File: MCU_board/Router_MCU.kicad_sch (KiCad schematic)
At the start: 72 parts, among them J1 Header, T1 HY601742, U1 MYC-YT507H, U2 TPS54340, U3 LAN8720A, X1 B4B-XH, X2 B4B-XH, X3 B4B-XH, X4 B4B-XH, X5 B2B-XH, X6 TFP09-2-12B, X7 RJ45, Y1 25MHz

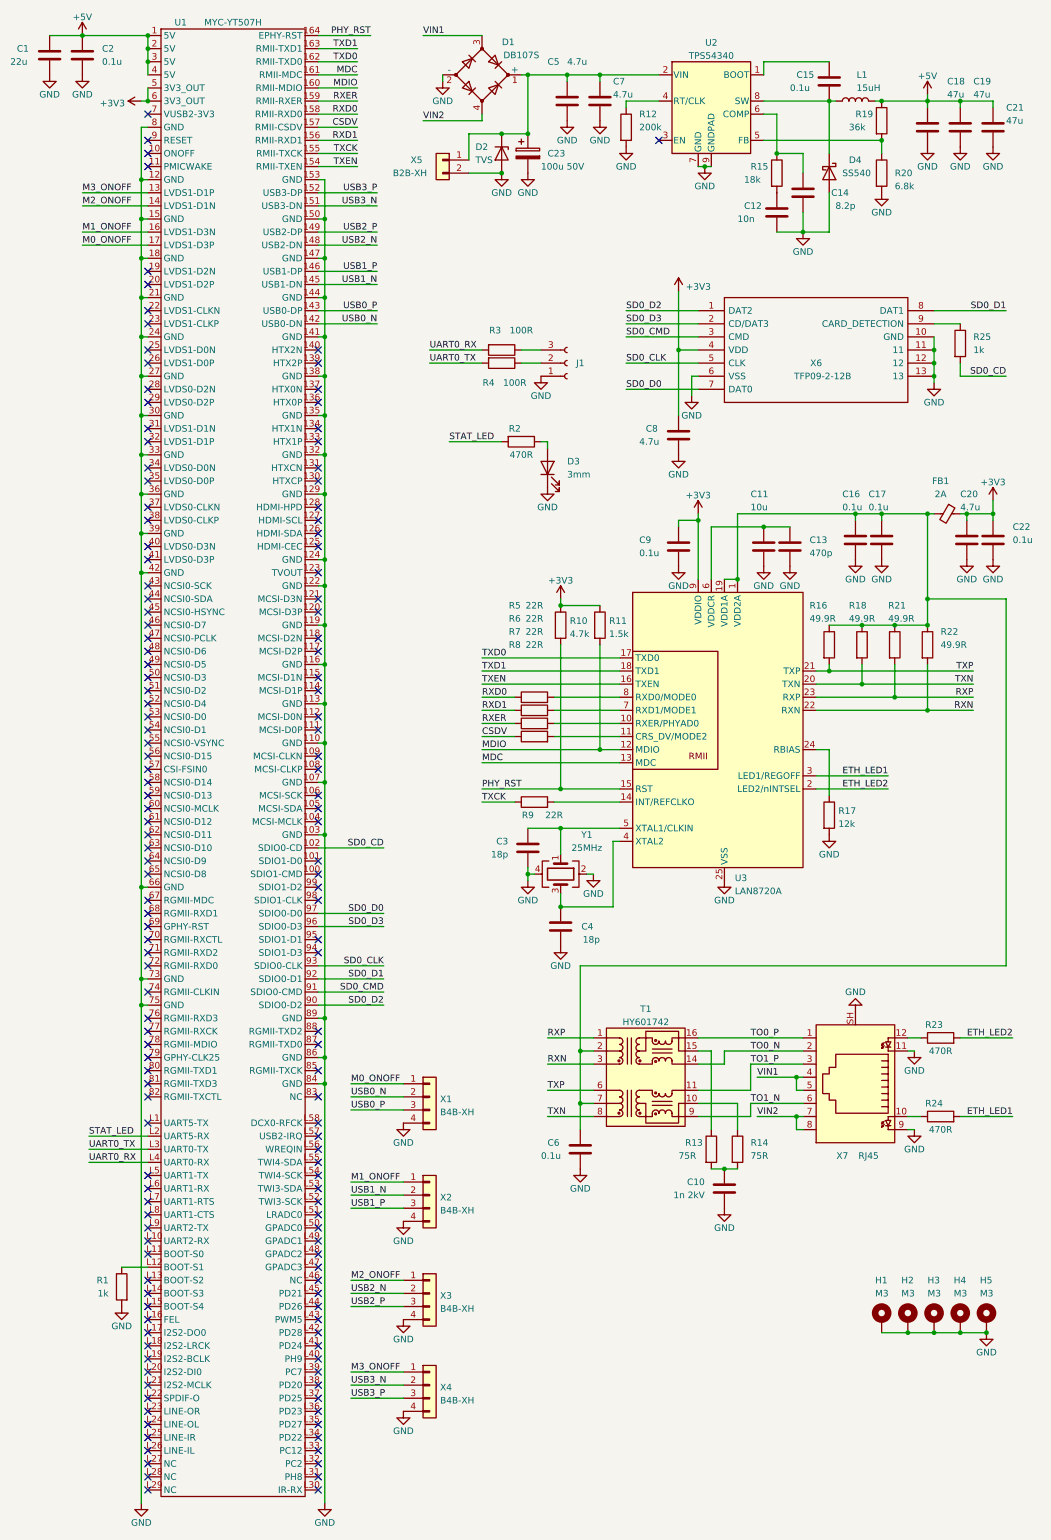
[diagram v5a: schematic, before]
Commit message: remove modems gpio ctrls
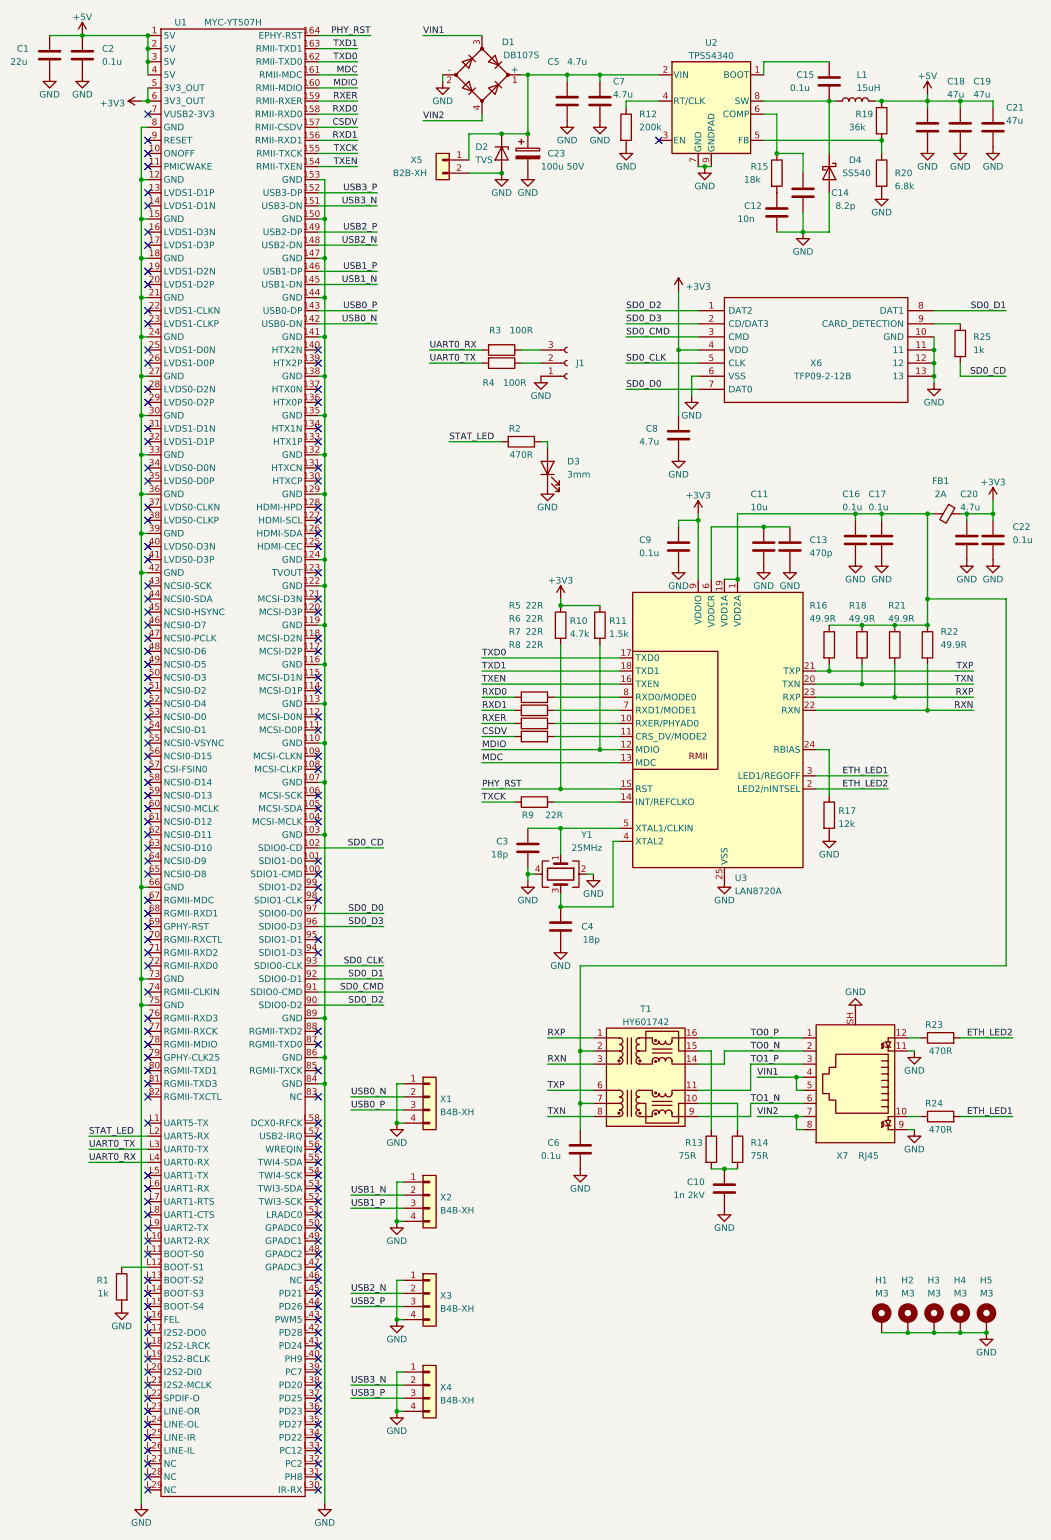
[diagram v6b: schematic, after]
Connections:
- net GND: now also X1.1 (Pin_1), X2.1 (Pin_1), X3.1 (Pin_1), X4.1 (Pin_1)
- net M0_ONOFF: no longer names the net of U1.17 (LVDS1-D3P)
- net M0_ONOFF: no longer X1.1 (Pin_1)
- net M1_ONOFF: no longer names the net of U1.16 (LVDS1-D3N)
- net M1_ONOFF: no longer X2.1 (Pin_1)
- net M2_ONOFF: no longer names the net of U1.14 (LVDS1-D1N)
- net M2_ONOFF: no longer X3.1 (Pin_1)
- net M3_ONOFF: no longer names the net of U1.13 (LVDS1-D1P)
- net M3_ONOFF: no longer X4.1 (Pin_1)
- no-connect marks 148 -> 152

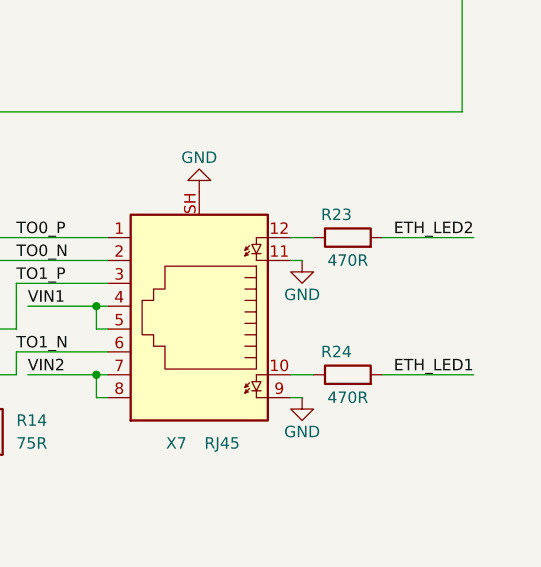
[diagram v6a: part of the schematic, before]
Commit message: lan8720 led config resistor
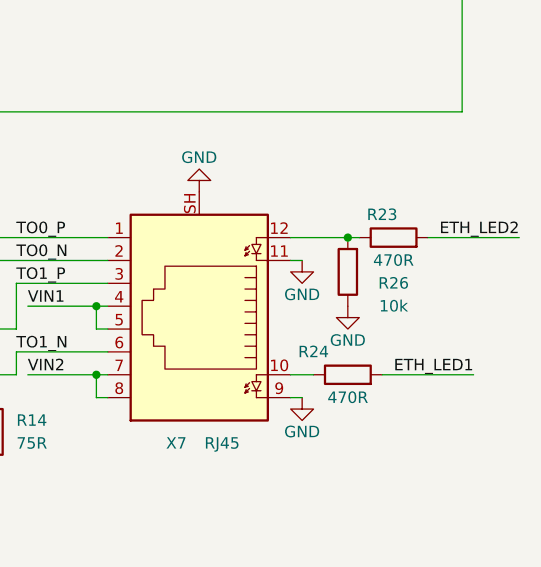
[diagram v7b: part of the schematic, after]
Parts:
- added R26: 10k, Resistor_SMD:R_0603_1608Metric, symbol Device:R
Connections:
- net GND: now also R26.1
- net at R23.1, X7.12: now also R26.2
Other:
- moved on the sheet: R23
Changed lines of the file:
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@@
   (junction (at 191.77 110.49) (diameter 0) (color 0 0 0 0)
   )
+  (junction (at 194.31 212.09) (diameter 0) (color 0 0 0 0)
+  )
   (junction (at 193.04 78.74) (diameter 0) (color 0 0 0 0)
   )
@@
     (stroke (width 0) (type default) (color 0 0 0 0))
   )
-  (wire (pts (xy 187.96 212.09) (xy 190.5 212.09))
+  (wire (pts (xy 187.96 212.09) (xy 194.31 212.09))
     (stroke (width 0) (type default) (color 0 0 0 0))
   )
@@
     (stroke (width 0) (type default) (color 0 0 0 0))
   )
-  (wire (pts (xy 198.12 212.09) (xy 208.28 212.09))
+  (wire (pts (xy 203.2 212.09) (xy 213.36 212.09))
     (stroke (width 0) (type default) (color 0 0 0 0))
   )
@@
     (stroke (width 0) (type default) (color 0 0 0 0))
   )
+  (wire (pts (xy 194.31 212.09) (xy 195.58 212.09))
+    (stroke (width 0) (type default) (color 0 0 0 0))
+  )
   (wire (pts (xy 167.64 52.07) (xy 167.64 55.88))
     (stroke (width 0) (type default) (color 0 0 0 0))
@@
     (effects (font (size 1.27 1.27)) (justify left bottom))
   )
-  (label "ETH_LED2" (at 208.28 212.09 180)
+  (label "ETH_LED2" (at 213.36 212.09 180)
     (effects (font (size 1.27 1.27)) (justify right bottom))
   )
@@
   (symbol (lib_id "Device:R") (at 194.31 227.33 90) (unit 1)
     (in_bom yes) (on_board yes)
-    (property "Reference" "R24" (id 0) (at 193.04 224.79 90))
+    (property "Reference" "R24" (id 0) (at 190.5 224.79 90))
     (property "Value" "470R" (id 1) (at 194.31 229.87 90))
     (property "Footprint" "Resistor_SMD:R_0603_1608Metric" (id 2) (at 194.31 229.108 90)
@@
     (pin "1")
   )
-  (symbol (lib_id "Device:R") (at 194.31 212.09 90) (unit 1)
+  (symbol (lib_id "Device:R") (at 199.39 212.09 90) (unit 1)
     (in_bom yes) (on_board yes)
-    (property "Reference" "R23" (id 0) (at 193.04 209.55 90))
-    (property "Value" "470R" (id 1) (at 194.31 214.63 90))
-    (property "Footprint" "Resistor_SMD:R_0603_1608Metric" (id 2) (at 194.31 213.868 90)
+    (property "Reference" "R23" (id 0) (at 198.12 209.55 90))
+    (property "Value" "470R" (id 1) (at 199.39 214.63 90))
+    (property "Footprint" "Resistor_SMD:R_0603_1608Metric" (id 2) (at 199.39 213.868 90)
       (effects (font (size 1.27 1.27)) hide)
     )
-    (property "Datasheet" "~" (id 3) (at 194.31 212.09 0)
+    (property "Datasheet" "~" (id 3) (at 199.39 212.09 0)
       (effects (font (size 1.27 1.27)) hide)
     )
@@
     (pin "1")
   )
+  (symbol (lib_id "Device:R") (at 194.31 215.9 180) (unit 1)
+    (in_bom yes) (on_board yes)
+    (property "Reference" "R26" (id 0) (at 199.39 217.17 0))
+    (property "Value" "10k" (id 1) (at 199.39 219.71 0))
+    (property "Footprint" "Resistor_SMD:R_0603_1608Metric" (id 2) (at 196.088 215.9 90)
+      (effects (font (size 1.27 1.27)) hide)
+    )
+    (property "Datasheet" "~" (id 3) (at 194.31 215.9 0)
+      (effects (font (size 1.27 1.27)) hide)
+    )
+    (pin "1")
+    (pin "2")
+  )
   (symbol (lib_id "Device:C") (at 143.51 116.84 0) (unit 1)
     (in_bom yes) (on_board yes)
@@
     (pin "2")
   )
+  (symbol (lib_id "power:GND") (at 194.31 219.71 0) (unit 1)
+    (in_bom yes) (on_board yes)
+    (property "Reference" "#PWR052" (id 0) (at 194.31 226.06 0)
+      (effects (font (size 1.27 1.27)) hide)
+    )
+    (property "Value" "GND" (id 1) (at 194.31 223.52 0))
+    (property "Footprint" "" (id 2) (at 194.31 219.71 0)
+      (effects (font (size 1.27 1.27)) hide)
+    )
+    (property "Datasheet" "" (id 3) (at 194.31 219.71 0)
+      (effects (font (size 1.27 1.27)) hide)
+    )
+    (pin "1")
+  )
   (symbol (lib_id "Connector:RJ45_LED_Shielded") (at 177.8 219.71 180) (unit 1)
     (in_bom yes) (on_board yes)
@@
       (reference "#PWR051") (unit 1) (value "GND") (footprint "")
     )
+    (path "/f8813757-0fd4-4165-a4da-c3ad51d8ba4e"
+      (reference "#PWR052") (unit 1) (value "GND") (footprint "")
+    )
     (path "/5f0d66a0-541f-44bb-b7f9-0e73e4c8da2e"
       (reference "C1") (unit 1) (value "22u") (footprint "Capacitor_SMD:C_0805_2012Metric")
@@
       (reference "R25") (unit 1) (value "1k") (footprint "Resistor_SMD:R_0603_1608Metric")
     )
+    (path "/9fecd989-e9df-4e49-bd09-c184a5fdfc7b"
+      (reference "R26") (unit 1) (value "10k") (footprint "Resistor_SMD:R_0603_1608Metric")
+    )
     (path "/d1da88a8-648f-4646-b2e2-3f88c274a6e7"
